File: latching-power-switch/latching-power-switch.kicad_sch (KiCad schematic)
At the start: 9 parts, among them Q1 2N3904, Q2 BS250, SW1 SW_Push

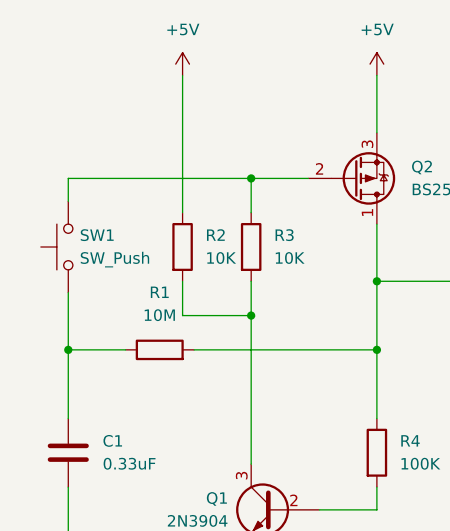
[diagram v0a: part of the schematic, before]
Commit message: update(latching-power-switch): add PCB layout
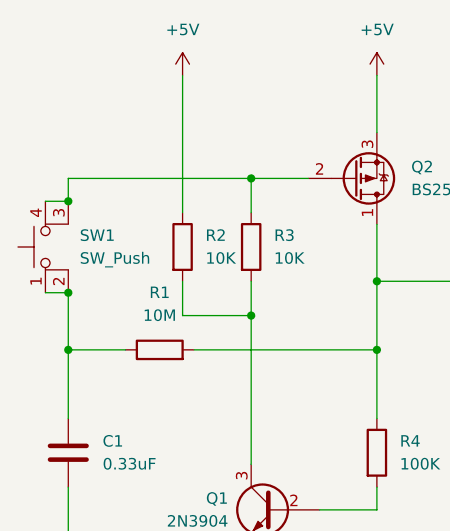
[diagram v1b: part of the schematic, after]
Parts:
- C1: footprint (none) -> Capacitor_THT:C_Disc_D5.0mm_W2.5mm_P5.00mm
- Q1, Q2: footprint Package_TO_SOT_THT:TO-92_Inline -> Package_TO_SOT_THT:TO-92_Inline_Wide
- R1, R3, R4, R5: footprint (none) -> Resistor_THT:R_Axial_DIN0207_L6.3mm_D2.5mm_P7.62mm_Horizontal
- R2: footprint (none) -> Resistor_THT:R_Axial_DIN0207_L6.3mm_D2.5mm_P10.16mm_Horizontal
- SW1: footprint (none) -> Button_Switch_THT:SW_PUSH_6mm; symbol Switch:SW_Push -> Switch:SW_MEC_5E
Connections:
- net at C1.1, R1.1, SW1.1: now also SW1.2
- net at Q2.2 (G), R3.1: now also SW1.3 (K), SW1.4 (A); no longer SW1.2
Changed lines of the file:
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@@
   (junction (at 151.13 92.71) (diameter 0) (color 0 0 0 0)
   )
+  (junction (at 105.41 93.98) (diameter 0) (color 0 0 0 0)
+  )
   (junction (at 125.73 96.52) (diameter 0) (color 0 0 0 0)
   )
   (junction (at 125.73 81.28) (diameter 0) (color 0 0 0 0)
   )
+  (junction (at 105.41 83.82) (diameter 0) (color 0 0 0 0)
+  )
   (junction (at 139.7 100.33) (diameter 0) (color 0 0 0 0)
   )
@@
     (stroke (width 0) (type default) (color 0 0 0 0))
   )
+  (wire (pts (xy 102.87 83.82) (xy 105.41 83.82))
+    (stroke (width 0) (type default) (color 0 0 0 0))
+  )
   (wire (pts (xy 151.13 115.57) (xy 151.13 127))
     (stroke (width 0) (type default) (color 0 0 0 0))
@@
   )
   (wire (pts (xy 125.73 123.19) (xy 125.73 127))
+    (stroke (width 0) (type default) (color 0 0 0 0))
+  )
+  (wire (pts (xy 102.87 93.98) (xy 105.41 93.98))
     (stroke (width 0) (type default) (color 0 0 0 0))
   )
@@
     (pin "1")
   )
-  (symbol (lib_id "Switch:SW_Push") (at 105.41 88.9 90) (unit 1)
+  (symbol (lib_id "Switch:SW_MEC_5E") (at 105.41 88.9 90) (unit 1)
     (in_bom yes) (on_board yes) (fields_autoplaced)
     (property "Reference" "SW1" (id 0) (at 106.68 87.6299 90)
@@
       (effects (font (size 1.27 1.27)) (justify right))
     )
-    (property "Footprint" "" (id 2) (at 100.33 88.9 0)
-      (effects (font (size 1.27 1.27)) hide)
-    )
-    (property "Datasheet" "~" (id 3) (at 100.33 88.9 0)
-      (effects (font (size 1.27 1.27)) hide)
-    )
-    (pin "1")
-    (pin "2")
+    (property "Footprint" "Button_Switch_THT:SW_PUSH_6mm" (id 2) (at 97.79 88.9 0)
+      (effects (font (size 1.27 1.27)) hide)
+    )
+    (property "Datasheet" "http://www.apem.com/int/index.php?controller=attachment&id_attachment=1371" (id 3) (at 97.79 88.9 0)
+      (effects (font (size 1.27 1.27)) hide)
+    )
+    (pin "1")
+    (pin "2")
+    (pin "3")
+    (pin "4")
   )
   (symbol (lib_id "Transistor_BJT:2N3904") (at 128.27 118.11 0) (mirror y) (unit 1)
@@
       (effects (font (size 1.27 1.27)) (justify left))
     )
-    (property "Footprint" "Package_TO_SOT_THT:TO-92_Inline" (id 2) (at 123.19 120.015 0)
+    (property "Footprint" "Package_TO_SOT_THT:TO-92_Inline_Wide" (id 2) (at 123.19 120.015 0)
       (effects (font (size 1.27 1.27) italic) (justify left) hide)
     )
@@
     (property "Reference" "R1" (id 0) (at 115.57 93.98 90))
     (property "Value" "10M" (id 1) (at 115.57 96.52 90))
-    (property "Footprint" "" (id 2) (at 115.57 102.108 90)
+    (property "Footprint" "Resistor_THT:R_Axial_DIN0207_L6.3mm_D2.5mm_P7.62mm_Horizontal" (id 2) (at 115.57 102.108 90)
       (effects (font (size 1.27 1.27)) hide)
     )
@@
       (effects (font (size 1.27 1.27)) (justify left))
     )
-    (property "Footprint" "" (id 2) (at 116.332 88.9 90)
+    (property "Footprint" "Resistor_THT:R_Axial_DIN0207_L6.3mm_D2.5mm_P10.16mm_Horizontal" (id 2) (at 116.332 88.9 90)
       (effects (font (size 1.27 1.27)) hide)
     )
@@
       (effects (font (size 1.27 1.27)) (justify left))
     )
-    (property "Footprint" "Package_TO_SOT_THT:TO-92_Inline" (id 2) (at 142.24 79.375 0)
+    (property "Footprint" "Package_TO_SOT_THT:TO-92_Inline_Wide" (id 2) (at 142.24 79.375 0)
       (effects (font (size 1.27 1.27) italic) (justify left) hide)
     )
@@
       (effects (font (size 1.27 1.27)) (justify left))
     )
-    (property "Footprint" "" (id 2) (at 123.952 88.9 90)
+    (property "Footprint" "Resistor_THT:R_Axial_DIN0207_L6.3mm_D2.5mm_P7.62mm_Horizontal" (id 2) (at 123.952 88.9 90)
       (effects (font (size 1.27 1.27)) hide)
     )
@@
       (effects (font (size 1.27 1.27)) (justify left))
     )
-    (property "Footprint" "" (id 2) (at 106.3752 115.57 0)
+    (property "Footprint" "Capacitor_THT:C_Disc_D5.0mm_W2.5mm_P5.00mm" (id 2) (at 106.3752 115.57 0)
       (effects (font (size 1.27 1.27)) hide)
     )
@@
       (effects (font (size 1.27 1.27)) (justify left))
     )
-    (property "Footprint" "" (id 2) (at 149.352 111.76 90)
+    (property "Footprint" "Resistor_THT:R_Axial_DIN0207_L6.3mm_D2.5mm_P7.62mm_Horizontal" (id 2) (at 149.352 111.76 90)
       (effects (font (size 1.27 1.27)) hide)
     )
@@
       (effects (font (size 1.27 1.27)) (justify left))
     )
-    (property "Footprint" "" (id 2) (at 137.922 111.76 90)
+    (property "Footprint" "Resistor_THT:R_Axial_DIN0207_L6.3mm_D2.5mm_P7.62mm_Horizontal" (id 2) (at 137.922 111.76 90)
       (effects (font (size 1.27 1.27)) hide)
     )
@@
     )
     (path "/c72ceef7-76b9-47b6-9edb-d5dadde82021"
-      (reference "C1") (unit 1) (value "0.33uF") (footprint "")
+      (reference "C1") (unit 1) (value "0.33uF") (footprint "Capacitor_THT:C_Disc_D5.0mm_W2.5mm_P5.00mm")
     )
     (path "/353da43b-2f48-49bd-b2b6-78006076697e"
-      (reference "Q1") (unit 1) (value "2N3904") (footprint "Package_TO_SOT_THT:TO-92_Inline")
+      (reference "Q1") (unit 1) (value "2N3904") (footprint "Package_TO_SOT_THT:TO-92_Inline_Wide")
     )
     (path "/a2593120-3cdd-4221-9716-9f28791e4cac"
-      (reference "Q2") (unit 1) (value "BS250") (footprint "Package_TO_SOT_THT:TO-92_Inline")
+      (reference "Q2") (unit 1) (value "BS250") (footprint "Package_TO_SOT_THT:TO-92_Inline_Wide")
     )
     (path "/5c78903e-c427-4aad-a53d-7f4ff9fd59bf"
-      (reference "R1") (unit 1) (value "10M") (footprint "")
+      (reference "R1") (unit 1) (value "10M") (footprint "Resistor_THT:R_Axial_DIN0207_L6.3mm_D2.5mm_P7.62mm_Horizontal")
     )
     (path "/9fe9cfd3-b04e-44ee-b5fc-dc4fb0fcd533"
-      (reference "R2") (unit 1) (value "10K") (footprint "")
+      (reference "R2") (unit 1) (value "10K") (footprint "Resistor_THT:R_Axial_DIN0207_L6.3mm_D2.5mm_P10.16mm_Horizontal")
     )
     (path "/b49b4664-eea2-49b8-b392-161ae5b6842f"
-      (reference "R3") (unit 1) (value "10K") (footprint "")
+      (reference "R3") (unit 1) (value "10K") (footprint "Resistor_THT:R_Axial_DIN0207_L6.3mm_D2.5mm_P7.62mm_Horizontal")
     )
     (path "/f0127f13-389a-434f-b1fd-5acd6c8bbab8"
-      (reference "R4") (unit 1) (value "100K") (footprint "")
+      (reference "R4") (unit 1) (value "100K") (footprint "Resistor_THT:R_Axial_DIN0207_L6.3mm_D2.5mm_P7.62mm_Horizontal")
     )
     (path "/e54f34c5-d663-4d97-8243-8575673eb8af"
-      (reference "R5") (unit 1) (value "10K") (footprint "")
+      (reference "R5") (unit 1) (value "10K") (footprint "Resistor_THT:R_Axial_DIN0207_L6.3mm_D2.5mm_P7.62mm_Horizontal")
     )
     (path "/1fe79091-91c9-4b48-ac92-ee75ae234bf2"
-      (reference "SW1") (unit 1) (value "SW_Push") (footprint "")
-    )
-  )
+      (reference "SW1") (unit 1) (value "SW_Push") (footprint "Button_Switch_THT:SW_PUSH_6mm")
+    )
+  )
